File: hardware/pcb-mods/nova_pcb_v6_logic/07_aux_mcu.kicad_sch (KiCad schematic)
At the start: 3 parts, among them J10 SSD1331_OLED, J11 WS2812B_Strip, U12 Arduino_Nano_v3.x

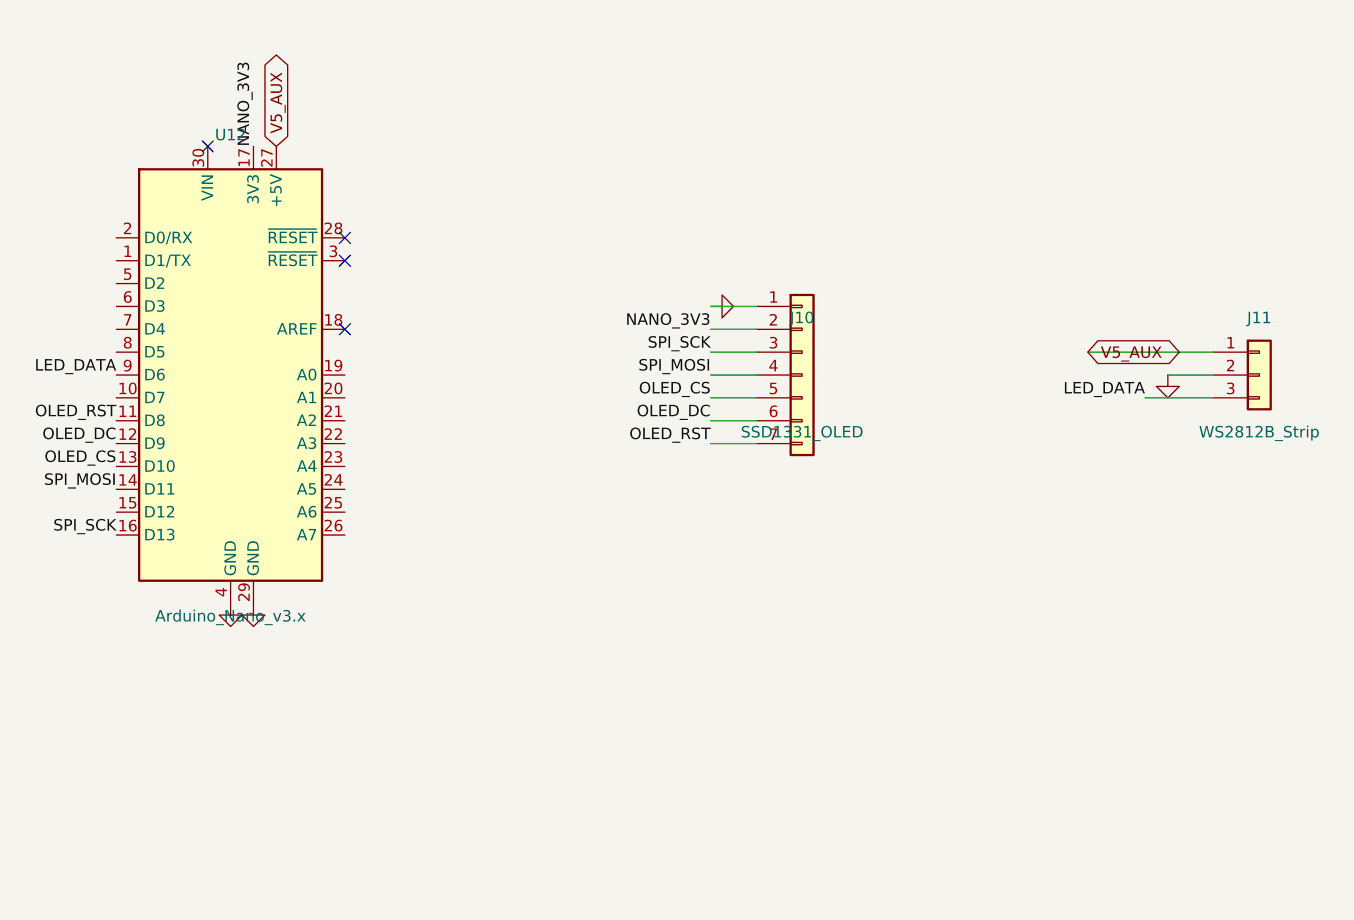
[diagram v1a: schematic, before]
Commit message: logic board: fix OLED (J10) power/pinout/level + add series-R protection
Fresh full-board review surfaced 3 real OLED issues vs the owned HiLetgo
SSD1331 (7-pin, VCC 2.8-5.5V):

1. J10 pin order had CS/RST crossed vs the module -> swapped board nets
   (J10.5=OLED_RST, J10.7=OLED_CS).
2. Vcc was on NANO_3V3 (Nano onboard reg, <=50mA, often absent when the
   Nano runs off its 5V pin) -> moved to V5_AUX (5V; in module's range).
3. Nano runs at 5V, so its SPI logic over-drives the 3.3V-regulated
   SSD1331 inputs -> added 5x 1k series R (R2-R6) on SCK/MOSI/RST/DC/CS.

Schematic: Device:R lib symbol + R2-R6 + _F nets bridging U12->R->J10,
ERC clean of new items. PCB: full Freerouting re-route, GND via added to
restitch U7.7 to the inner plane, DRC 0/0, gerbers re-cut.

Also verified this pass: Teensy footprint pad->pin map (firmware pins
correct), bus Pattern B path, BATT_LOW cross-board (3.3V pull, correct
polarity), e-stop polarity consistent power<->logic. Both boards DRC 0/0.

Co-Authored-By: Claude Opus 4.8 <noreply@anthropic.com>
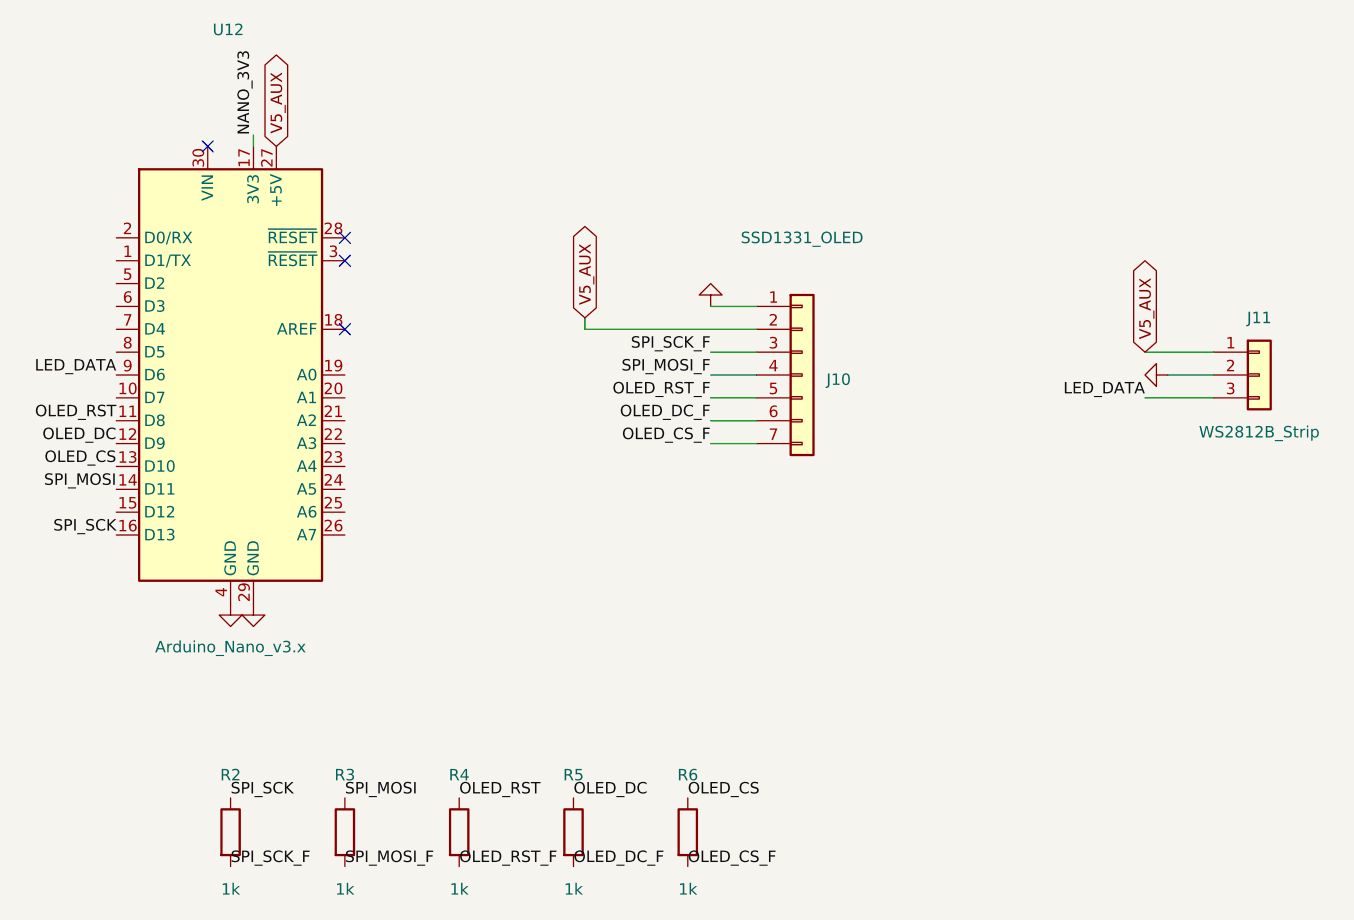
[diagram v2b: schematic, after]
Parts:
- added R2, R3, R4, R5, R6: 1k, Resistor_SMD:R_0603_1608Metric, symbol Device:R
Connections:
- net NANO_3V3: no longer J10.2 (Pin_2)
- net OLED_CS: now also R6.1; no longer J10.5 (Pin_5)
- net OLED_DC: now also R5.1; no longer J10.6 (Pin_6)
- net OLED_RST: now also R4.1; no longer J10.7 (Pin_7)
- net SPI_MOSI: now also R3.1; no longer J10.4 (Pin_4)
- net SPI_SCK: now also R2.1; no longer J10.3 (Pin_3)
- net V5_AUX: now also J10.2 (Pin_2)
- new net OLED_CS_F: J10.7 (Pin_7), R6.2
- new net OLED_DC_F: J10.6 (Pin_6), R5.2
- new net OLED_RST_F: J10.5 (Pin_5), R4.2
- new net SPI_MOSI_F: J10.4 (Pin_4), R3.2
- new net SPI_SCK_F: J10.3 (Pin_3), R2.2
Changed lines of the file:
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@@
-	(wire
-		(pts
-			(xy 109.22 71.12) (xy 104.14 71.12)
-		)
-		(stroke
-			(width 0)
-			(type default)
-		)
-	)
 	(wire
 		(pts
@@
 	(wire
 		(pts
-			(xy 160.02 73.66) (xy 146.05 73.66)
+			(xy 53.34 49.53) (xy 53.34 50.8)
+		)
+		(stroke
+			(width 0)
+			(type default)
+		)
+	)
+	(wire
+		(pts
+			(xy 160.02 73.66) (xy 152.4 73.66)
+		)
+		(stroke
+			(width 0)
+			(type default)
+		)
+	)
+	(wire
+		(pts
+			(xy 90.17 71.12) (xy 109.22 71.12)
 		)
 		(stroke
@@
 	(wire
 		(pts
+			(xy 90.17 71.12) (xy 90.17 69.85)
+		)
+		(stroke
+			(width 0)
+			(type default)
+		)
+	)
+	(wire
+		(pts
 			(xy 109.22 76.2) (xy 104.14 76.2)
 		)
@@
 		)
 	)
-	(label "OLED_CS"
+	(label "OLED_RST_F"
 		(at 104.14 78.74 180)
 		(effects
@@
 		)
 	)
-	(label "OLED_DC"
+	(label "OLED_DC_F"
 		(at 104.14 81.28 180)
 		(effects
@@
 	)
 	(label "NANO_3V3"
-		(at 53.34 50.8 90)
+		(at 53.34 49.53 90)
 		(effects
 			(font
@@
 		)
 	)
-	(label "OLED_RST"
+	(label "OLED_CS_F"
 		(at 104.14 83.82 180)
 		(effects
@@
 		)
 	)
-	(label "SPI_MOSI"
+	(label "SPI_MOSI_F"
 		(at 104.14 76.2 180)
 		(effects
@@
 		)
 	)
-	(label "SPI_SCK"
+	(label "SPI_SCK_F"
 		(at 104.14 73.66 180)
-		(effects
-			(font
-				(size 1.27 1.27)
-			)
-			(justify right bottom)
-		)
-	)
-	(label "NANO_3V3"
-		(at 104.14 71.12 180)
 		(effects
 			(font
@@
 	(global_label "V5_AUX"
 		(shape bidirectional)
-		(at 146.05 73.66 0)
+		(at 152.4 73.66 90)
 		(effects
 			(font
@@
 		)
 		(property "Intersheetrefs" "${INTERSHEET_REFS}"
-			(at 146.05 73.66 0)
+			(at 152.4 73.66 90)
 			(effects
 				(font
@@
 		(property "Intersheetrefs" "${INTERSHEET_REFS}"
 			(at 55.88 50.8 90)
+			(effects
+				(font
+					(size 1.27 1.27)
+				)
+				(hide yes)
+			)
+		)
+	)
+	(global_label "V5_AUX"
+		(shape bidirectional)
+		(at 90.17 69.85 90)
+		(effects
+			(font
+				(size 1.27 1.27)
+			)
+			(justify left)
+		)
+		(property "Intersheetrefs" "${INTERSHEET_REFS}"
+			(at 90.17 69.85 90)
 			(effects
 				(font
@@
 		(dnp no)
 		(property "Reference" "U12"
-			(at 50.8 49.53 0)
+			(at 50.546 37.846 0)
 			(effects
 				(font
@@
 		)
 		(property "Value" "Arduino_Nano_v3.x"
-			(at 50.8 103 0)
+			(at 50.8 106.426 0)
 			(effects
 				(font
@@
 	(symbol
 		(lib_id "power:GND")
-		(at 104.14 68.58 90)
+		(at 104.14 68.58 180)
 		(unit 1)
 		(exclude_from_sim no)
@@
 		(dnp no)
 		(property "Reference" "#PWR71"
-			(at 104.14 62.23 270)
+			(at 97.79 68.58 270)
 			(effects
 				(font
@@
 		)
 		(property "Value" "GND"
-			(at 104.14 74.93 270)
+			(at 110.49 68.58 270)
 			(effects
 				(font
@@
 	(symbol
 		(lib_id "power:GND")
-		(at 154.94 76.2 0)
+		(at 154.94 76.2 270)
 		(unit 1)
 		(exclude_from_sim no)
@@
 		(dnp no)
 		(property "Reference" "#PWR72"
-			(at 161.29 76.2 270)
+			(at 154.94 82.55 270)
 			(effects
 				(font
@@
 		)
 		(property "Value" "GND"
-			(at 148.59 76.2 270)
+			(at 154.94 69.85 270)
 			(effects
 				(font
@@
 		(dnp no)
 		(property "Reference" "J10"
-			(at 114.3 69.85 0)
+			(at 118.364 76.708 0)
 			(effects
 				(font
@@
 		)
 		(property "Value" "SSD1331_OLED"
-			(at 114.3 82.55 0)
+			(at 114.3 60.96 0)
 			(effects
 				(font
@@
 		)
 	)
+	(symbol
+		(lib_id "Device:R")(at 50.8 127.0 0)(unit 1)
+		(exclude_from_sim no)(in_bom yes)(on_board yes)(dnp no)
+		(property "Reference" "R2" (at 50.8 120.65 0)(effects (font (size 1.27 1.27))))
+		(property "Value" "1k" (at 50.8 133.35 0)(effects (font (size 1.27 1.27))))
+		(property "Footprint" "Resistor_SMD:R_0603_1608Metric" (at 50.8 127.0 0)(effects (font (size 1.27 1.27))(hide yes)))
+		(property "Datasheet" "~" (at 50.8 127.0 0)(effects (font (size 1.27 1.27))(hide yes)))
+		(property "Description" "" (at 50.8 127.0 0)(effects (font (size 1.27 1.27))))
+		(pin "1")
+		(pin "2")
+		(instances (project "nova_pcb_v6_logic" (path "/f535083b-f621-4317-a378-cf746e7f972b/0af7f1f2-3a0a-4436-aaa7-f191048b3c83" (reference "R2")(unit 1))))
+	)
+	(label "SPI_SCK" (at 50.8 123.19 0)(effects (font (size 1.27 1.27))(justify left bottom)))
+	(label "SPI_SCK_F" (at 50.8 130.81 0)(effects (font (size 1.27 1.27))(justify left bottom)))
+	(symbol
+		(lib_id "Device:R")(at 63.5 127.0 0)(unit 1)
+		(exclude_from_sim no)(in_bom yes)(on_board yes)(dnp no)
+		(property "Reference" "R3" (at 63.5 120.65 0)(effects (font (size 1.27 1.27))))
+		(property "Value" "1k" (at 63.5 133.35 0)(effects (font (size 1.27 1.27))))
+		(property "Footprint" "Resistor_SMD:R_0603_1608Metric" (at 63.5 127.0 0)(effects (font (size 1.27 1.27))(hide yes)))
+		(property "Datasheet" "~" (at 63.5 127.0 0)(effects (font (size 1.27 1.27))(hide yes)))
+		(property "Description" "" (at 63.5 127.0 0)(effects (font (size 1.27 1.27))))
+		(pin "1")
+		(pin "2")
+		(instances (project "nova_pcb_v6_logic" (path "/f535083b-f621-4317-a378-cf746e7f972b/0af7f1f2-3a0a-4436-aaa7-f191048b3c83" (reference "R3")(unit 1))))
+	)
+	(label "SPI_MOSI" (at 63.5 123.19 0)(effects (font (size 1.27 1.27))(justify left bottom)))
+	(label "SPI_MOSI_F" (at 63.5 130.81 0)(effects (font (size 1.27 1.27))(justify left bottom)))
+	(symbol
+		(lib_id "Device:R")(at 76.2 127.0 0)(unit 1)
+		(exclude_from_sim no)(in_bom yes)(on_board yes)(dnp no)
+		(property "Reference" "R4" (at 76.2 120.65 0)(effects (font (size 1.27 1.27))))
+		(property "Value" "1k" (at 76.2 133.35 0)(effects (font (size 1.27 1.27))))
+		(property "Footprint" "Resistor_SMD:R_0603_1608Metric" (at 76.2 127.0 0)(effects (font (size 1.27 1.27))(hide yes)))
+		(property "Datasheet" "~" (at 76.2 127.0 0)(effects (font (size 1.27 1.27))(hide yes)))
+		(property "Description" "" (at 76.2 127.0 0)(effects (font (size 1.27 1.27))))
+		(pin "1")
+		(pin "2")
+		(instances (project "nova_pcb_v6_logic" (path "/f535083b-f621-4317-a378-cf746e7f972b/0af7f1f2-3a0a-4436-aaa7-f191048b3c83" (reference "R4")(unit 1))))
+	)
+	(label "OLED_RST" (at 76.2 123.19 0)(effects (font (size 1.27 1.27))(justify left bottom)))
+	(label "OLED_RST_F" (at 76.2 130.81 0)(effects (font (size 1.27 1.27))(justify left bottom)))
+	(symbol
+		(lib_id "Device:R")(at 88.9 127.0 0)(unit 1)
+		(exclude_from_sim no)(in_bom yes)(on_board yes)(dnp no)
+		(property "Reference" "R5" (at 88.9 120.65 0)(effects (font (size 1.27 1.27))))
+		(property "Value" "1k" (at 88.9 133.35 0)(effects (font (size 1.27 1.27))))
+		(property "Footprint" "Resistor_SMD:R_0603_1608Metric" (at 88.9 127.0 0)(effects (font (size 1.27 1.27))(hide yes)))
+		(property "Datasheet" "~" (at 88.9 127.0 0)(effects (font (size 1.27 1.27))(hide yes)))
+		(property "Description" "" (at 88.9 127.0 0)(effects (font (size 1.27 1.27))))
+		(pin "1")
+		(pin "2")
+		(instances (project "nova_pcb_v6_logic" (path "/f535083b-f621-4317-a378-cf746e7f972b/0af7f1f2-3a0a-4436-aaa7-f191048b3c83" (reference "R5")(unit 1))))
+	)
+	(label "OLED_DC" (at 88.9 123.19 0)(effects (font (size 1.27 1.27))(justify left bottom)))
+	(label "OLED_DC_F" (at 88.9 130.81 0)(effects (font (size 1.27 1.27))(justify left bottom)))
+	(symbol
+		(lib_id "Device:R")(at 101.6 127.0 0)(unit 1)
+		(exclude_from_sim no)(in_bom yes)(on_board yes)(dnp no)
+		(property "Reference" "R6" (at 101.6 120.65 0)(effects (font (size 1.27 1.27))))
+		(property "Value" "1k" (at 101.6 133.35 0)(effects (font (size 1.27 1.27))))
+		(property "Footprint" "Resistor_SMD:R_0603_1608Metric" (at 101.6 127.0 0)(effects (font (size 1.27 1.27))(hide yes)))
+		(property "Datasheet" "~" (at 101.6 127.0 0)(effects (font (size 1.27 1.27))(hide yes)))
+		(property "Description" "" (at 101.6 127.0 0)(effects (font (size 1.27 1.27))))
+		(pin "1")
+		(pin "2")
+		(instances (project "nova_pcb_v6_logic" (path "/f535083b-f621-4317-a378-cf746e7f972b/0af7f1f2-3a0a-4436-aaa7-f191048b3c83" (reference "R6")(unit 1))))
+	)
+	(label "OLED_CS" (at 101.6 123.19 0)(effects (font (size 1.27 1.27))(justify left bottom)))
+	(label "OLED_CS_F" (at 101.6 130.81 0)(effects (font (size 1.27 1.27))(justify left bottom)))
 	(sheet_instances
 		(path "/"

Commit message: logic board: clear ERC (no_connects, drop unused NANO_3V3 + redundant V5_AUX PWR_FLAG)
ERC 18 errors -> 0 (2 cosmetic lib_symbol_mismatch warnings remain, board=truth).

- 07_aux_mcu: add no_connect on 16 unused Arduino Nano GPIO + pin 17 (3V3).
  Remove the floating NANO_3V3 label + its stub wire: the Nano's 3V3 output
  drives nothing (verified - OLED runs on V5_AUX/5V, +3V3 is Teensy-sourced).
- 09_interboard: remove redundant #FLG20 PWR_FLAG on V5_AUX (conflicted with
  the Nano +5V power-output pin -> pin_to_pin) + its orphaned V5_AUX label.

Board copper unchanged (schematic annotations only). The committed .kicad_pcb
was already clean (1x R7); the duplicate-R7 + 11 DRC violations existed only in
the uncommitted working tree and have been reverted. Gerbers refreshed from the
clean board.

Co-Authored-By: Claude Opus 4.8 <noreply@anthropic.com>
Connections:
- net NANO_3V3: no longer names the net of U12.17 (3V3)
- no-connect marks 4 -> 21
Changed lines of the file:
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@@
 	(wire
 		(pts
-			(xy 53.34 49.53) (xy 53.34 50.8)
+			(xy 160.02 73.66) (xy 152.4 73.66)
 		)
 		(stroke
@@
 	(wire
 		(pts
-			(xy 160.02 73.66) (xy 152.4 73.66)
+			(xy 90.17 71.12) (xy 109.22 71.12)
 		)
 		(stroke
@@
 	(wire
 		(pts
-			(xy 90.17 71.12) (xy 109.22 71.12)
+			(xy 109.22 83.82) (xy 104.14 83.82)
 		)
 		(stroke
@@
 	(wire
 		(pts
-			(xy 109.22 83.82) (xy 104.14 83.82)
+			(xy 90.17 71.12) (xy 90.17 69.85)
 		)
 		(stroke
@@
 	(wire
 		(pts
-			(xy 90.17 71.12) (xy 90.17 69.85)
+			(xy 109.22 76.2) (xy 104.14 76.2)
 		)
 		(stroke
@@
 	(wire
 		(pts
-			(xy 109.22 76.2) (xy 104.14 76.2)
+			(xy 109.22 68.58) (xy 104.14 68.58)
 		)
 		(stroke
@@
 	(wire
 		(pts
-			(xy 109.22 68.58) (xy 104.14 68.58)
+			(xy 160.02 78.74) (xy 152.4 78.74)
 		)
 		(stroke
@@
 		)
 	)
-	(wire
-		(pts
-			(xy 160.02 78.74) (xy 152.4 78.74)
-		)
-		(stroke
-			(width 0)
-			(type default)
-		)
-	)
 	(label "OLED_RST_F"
 		(at 104.14 78.74 180)
@@
 			)
 			(justify right bottom)
-		)
-	)
-	(label "NANO_3V3"
-		(at 53.34 49.53 90)
-		(effects
-			(font
-				(size 1.27 1.27)
-			)
-			(justify left bottom)
 		)
 	)
@@
 	(label "OLED_CS" (at 101.6 123.19 0)(effects (font (size 1.27 1.27))(justify left bottom)))
 	(label "OLED_CS_F" (at 101.6 130.81 0)(effects (font (size 1.27 1.27))(justify left bottom)))
+	(no_connect
+		(at 38.1 60.96)
+	)
+	(no_connect
+		(at 38.1 63.5)
+	)
+	(no_connect
+		(at 38.1 66.04)
+	)
+	(no_connect
+		(at 38.1 68.58)
+	)
+	(no_connect
+		(at 38.1 71.12)
+	)
+	(no_connect
+		(at 38.1 73.66)
+	)
+	(no_connect
+		(at 38.1 78.74)
+	)
+	(no_connect
+		(at 38.1 91.44)
+	)
+	(no_connect
+		(at 63.5 76.2)
+	)
+	(no_connect
+		(at 63.5 78.74)
+	)
+	(no_connect
+		(at 63.5 81.28)
+	)
+	(no_connect
+		(at 63.5 83.82)
+	)
+	(no_connect
+		(at 63.5 86.36)
+	)
+	(no_connect
+		(at 63.5 88.9)
+	)
+	(no_connect
+		(at 63.5 91.44)
+	)
+	(no_connect
+		(at 63.5 93.98)
+	)
+	(no_connect
+		(at 53.34 50.8)
+	)
 	(sheet_instances
 		(path "/"
